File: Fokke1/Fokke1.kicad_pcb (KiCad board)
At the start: 2 copper layers, 209 x 112 mm, 101 parts, among them J101 Conn_01x20_Male, J11 Conn_01x05_Male, J12 Conn_01x05_Male, J401 Conn_01x10_Male, J403 Conn_01x10_Male, SW101 SW_SPST, SW102 SW_SPST, SW103 SW_SPST, SW104 SW_SPST, SW105 SW_SPST, SW106 SW_SPST, SW107 SW_SPST, SW108 SW_SPST, SW109 SW_SPST, SW11 SW_SPST, U11 MAX485E, U12 24LC256, U13 ATmega328-A, U14 HEADER_3x2, U26 L78L05_SOT89, U501 XC6206PxxxMR, Y11 crystal_arduino

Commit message: added logo and layout plans
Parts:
- removed C11: 100n, Capacitor_SMD:C_0603_1608Metric_Pad1.08x0.95mm_HandSolder
- removed C12, C30: 100nF, Capacitor_SMD:C_0603_1608Metric_Pad1.08x0.95mm_HandSolder
- removed C13, C14: 12pF, Capacitor_SMD:C_0402_1005Metric_Pad0.74x0.62mm_HandSolder
- removed C29: 330nF, Capacitor_SMD:C_0603_1608Metric_Pad1.08x0.95mm_HandSolder
- removed C31: 100uF, Capacitor_SMD:C_1206_3216Metric_Pad1.33x1.80mm_HandSolder
- removed C501, C502: 1uF, Capacitor_SMD:C_0603_1608Metric_Pad1.08x0.95mm_HandSolder
- removed D11: LED, LED_SMD:LED_0805_2012Metric_Pad1.15x1.40mm_HandSolder
- removed J101: Conn_01x20_Male, Connector_PinHeader_2.54mm:PinHeader_1x20_P2.54mm_Vertical
- removed J11, J12: Conn_01x05_Male, custom_kicad_lib_sk:castellated_2.54mm_01x06
- removed J401, J403: Conn_01x10_Male, custom_kicad_lib_sk:castellated_2.54mm_01x10
- removed R101, R102, R103, R104, R107, R108, R109: R, Resistor_SMD:R_0805_2012Metric_Pad1.20x1.40mm_HandSolder
- removed R11, R13: 10k, Resistor_SMD:R_0402_1005Metric_Pad0.72x0.64mm_HandSolder
- removed R12: 6k2, Resistor_SMD:R_0603_1608Metric_Pad0.98x0.95mm_HandSolder
- removed R301, R302, R303: 10k, Resistor_SMD:R_0402_1005Metric
- removed R601, R602: 4k7, Resistor_SMD:R_0603_1608Metric
- removed the REF** at (32.5, 129.5)
- removed the REF** at (173.0, 129.5)
- removed the REF** at (234.5, 72.5)
- removed the REF** at (32.5, 72.5)
- removed the REF** at (234.5, 129.5)
- removed the REF** at (100.0, 72.5)
- removed the REF** at (100.0, 129.5)
- removed the REF** at (173.0, 72.5)
- removed the REF** at (200.0, 123.0)
- removed SW11: SW_SPST, Button_Switch_SMD:SW_SPST_SKQG_WithStem
- removed U11: MAX485E, Package_SO:SOIC-8_3.9x4.9mm_P1.27mm
- removed U12: 24LC256, Package_SO:SOIC-8_3.9x4.9mm_P1.27mm
- removed U13: ATmega328-A, Package_QFP:TQFP-32_7x7mm_P0.8mm
- removed U14: HEADER_3x2, Connector_PinSocket_1.27mm:PinSocket_2x03_P1.27mm_Vertical
- removed U26: L78L05_SOT89, Package_TO_SOT_SMD:SOT-89-3
- removed U501: XC6206PxxxMR, Package_TO_SOT_SMD:SOT-23
- removed Y11: crystal_arduino, custom_kicad_lib_sk:crystal_arduino
- added G***: LOGO, kicad_images:Train-Science logo small, F.Cu at (36.0, 120.5)
- added REF**: PinHeader_2x20_P2.00mm_Vertical_SMD, Connector_PinHeader_2.00mm:PinHeader_2x20_P2.00mm_Vertical_SMD, B.Cu at (122.5, 83.5)
- R105: value R -> 100R
- moved R105 77.3 mm to (220.8, 115.5)
- moved R106 76.1 mm to (221.0, 121.0)
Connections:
- D106 pad 1: (no net) -> GPIO6 (x16)
- D106 pad 2: (no net) -> Net-(D106-Pad2) (x16)
- D107 pad 1: (no net) -> GPIO7 (x4)
- D107 pad 2: (no net) -> Net-(D107-Pad2) (x4)
- D109 pad 1: (no net) -> GPIO9 (x5)
- D109 pad 2: (no net) -> Net-(D109-Pad2) (x5)
- SW101 pad 1: (no net) -> GND (x3)
- SW101 pad 2: (no net) -> GPIO1 (x3)
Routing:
- net (no net): track 237.6 -> 0.00 mm, vias 12 -> 0
- net +5V: track 97.1 -> 0.00 mm, vias 7 -> 0
- net GPIO11: track 18.8 -> 0.00 mm
- net GPIO2: track 18.8 -> 0.00 mm, vias 2 -> 0
- net GPIO6: track 16.5 -> 0.00 mm
- net GPIO5: track 16.3 -> 0.00 mm
- net GPIO13: track 15.9 -> 0.00 mm, vias 2 -> 0
- net GPIO9: track 15.6 -> 0.00 mm, vias 2 -> 0
- net GPIO7: track 15.6 -> 0.00 mm
- net GPIO8: track 14.7 -> 0.00 mm
- net GPIO12: track 13.3 -> 0.00 mm, vias 2 -> 0
- net GPIO3: track 12.7 -> 0.00 mm
- net GPIO4: track 10.8 -> 0.00 mm
- net GPIO10: track 9.35 -> 0.00 mm
- net +3V3: track 8.18 -> 0.00 mm
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- removed copper zone on B.Cu, net GND
- removed copper zone on F.Cu, net GND
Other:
- board size 209 x 112 mm -> 209 x 64 mm
- board text removed: "3V3"
- board text removed: "5V"
- board text removed: "A"
- board text removed: "A0"
- board text removed: "A1"
- board text removed: "A2"
- board text removed: "A3"
- board text removed: "B"
- board text removed: "D10"
- board text removed: "D11"
- board text removed: "D12"
- board text removed: "D13"
- board text removed: "D2"
- board text removed: "D3"
- board text removed: "D4"
- board text removed: "D5"
- board text removed: "D6"
- board text removed: "D7"
- board text removed: "D8"
- board text removed: "D9"
- board text removed: "GND"
- board text removed: "ICSP"
- board text removed: "RES"
- board text removed: "RX"
- board text removed: "SCL"
- board text removed: "SDA"
- board text removed: "TX"
- board text removed: "Train-Science"
- board text removed: "Vin"

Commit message: I am halfway of schematic of Fokke1. I need to make me new footprints for leds and resistors and switches because I want to remove and add certain silk texts
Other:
- board text added: "1"
- board text added: "10"
- board text added: "11"
- board text added: "12"
- board text added: "2"
- board text added: "3"
- board text added: "4"
- board text added: "5"
- board text added: "6"
- board text added: "7"
- board text added: "8"
- board text added: "9"
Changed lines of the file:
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@@
   (gr_rect (start 30 76) (end 237 126) (layer "F.SilkS") (width 0.15) (fill none))
   (gr_rect (start 238 69) (end 29 133) (layer "Edge.Cuts") (width 0.1) (fill none))
+  (gr_text "10" (at 187.5 124.5) (layer "Dwgs.User")
+    (effects (font (size 1 1) (thickness 0.15)))
+  )
+  (gr_text "7" (at 161 94.5) (layer "Dwgs.User")
+    (effects (font (size 1 1) (thickness 0.15)))
+  )
+  (gr_text "9" (at 197.5 118) (layer "Dwgs.User")
+    (effects (font (size 1 1) (thickness 0.15)))
+  )
+  (gr_text "10" (at 190.5 88.5) (layer "Dwgs.User")
+    (effects (font (size 1 1) (thickness 0.15)))
+  )
+  (gr_text "1" (at 58 94) (layer "Dwgs.User")
+    (effects (font (size 1 1) (thickness 0.15)))
+  )
+  (gr_text "7" (at 154 80) (layer "Dwgs.User")
+    (effects (font (size 1 1) (thickness 0.15)))
+  )
+  (gr_text "6" (at 100 109) (layer "Dwgs.User")
+    (effects (font (size 1 1) (thickness 0.15)))
+  )
+  (gr_text "5" (at 142.5 102) (layer "Dwgs.User")
+    (effects (font (size 1 1) (thickness 0.15)))
+  )
+  (gr_text "12" (at 232 101.5) (layer "Dwgs.User")
+    (effects (font (size 1 1) (thickness 0.15)))
+  )
+  (gr_text "11" (at 232 80.5) (layer "Dwgs.User")
+    (effects (font (size 1 1) (thickness 0.15)))
+  )
+  (gr_text "4" (at 64.5 113) (layer "Dwgs.User")
+    (effects (font (size 1 1) (thickness 0.15)))
+  )
+  (gr_text "4" (at 147 93.5) (layer "Dwgs.User")
+    (effects (font (size 1 1) (thickness 0.15)))
+  )
+  (gr_text "8" (at 192.5 100.5) (layer "Dwgs.User")
+    (effects (font (size 1 1) (thickness 0.15)))
+  )
+  (gr_text "2" (at 39 109.5) (layer "Dwgs.User")
+    (effects (font (size 1 1) (thickness 0.15)))
+  )
+  (gr_text "1" (at 39 89.5) (layer "Dwgs.User")
+    (effects (font (size 1 1) (thickness 0.15)))
+  )
+  (gr_text "2" (at 74.5 106.5) (layer "Dwgs.User")
+    (effects (font (size 1 1) (thickness 0.15)))
+  )
+  (gr_text "6" (at 152 100.5) (layer "Dwgs.User")
+    (effects (font (size 1 1) (thickness 0.15)))
+  )
+  (gr_text "3" (at 111.5 117) (layer "Dwgs.User")
+    (effects (font (size 1 1) (thickness 0.15)))
+  )
+  (gr_text "5" (at 99.5 90) (layer "Dwgs.User")
+    (effects (font (size 1 1) (thickness 0.15)))
+  )
+  (gr_text "9" (at 148.5 122) (layer "Dwgs.User")
+    (effects (font (size 1 1) (thickness 0.15)))
+  )
+  (gr_text "3" (at 68 87) (layer "Dwgs.User")
+    (effects (font (size 1 1) (thickness 0.15)))
+  )
+  (gr_text "8\n" (at 170.980384 98.945766) (layer "Dwgs.User")
+    (effects (font (size 1 1) (thickness 0.15)))
+  )
 )

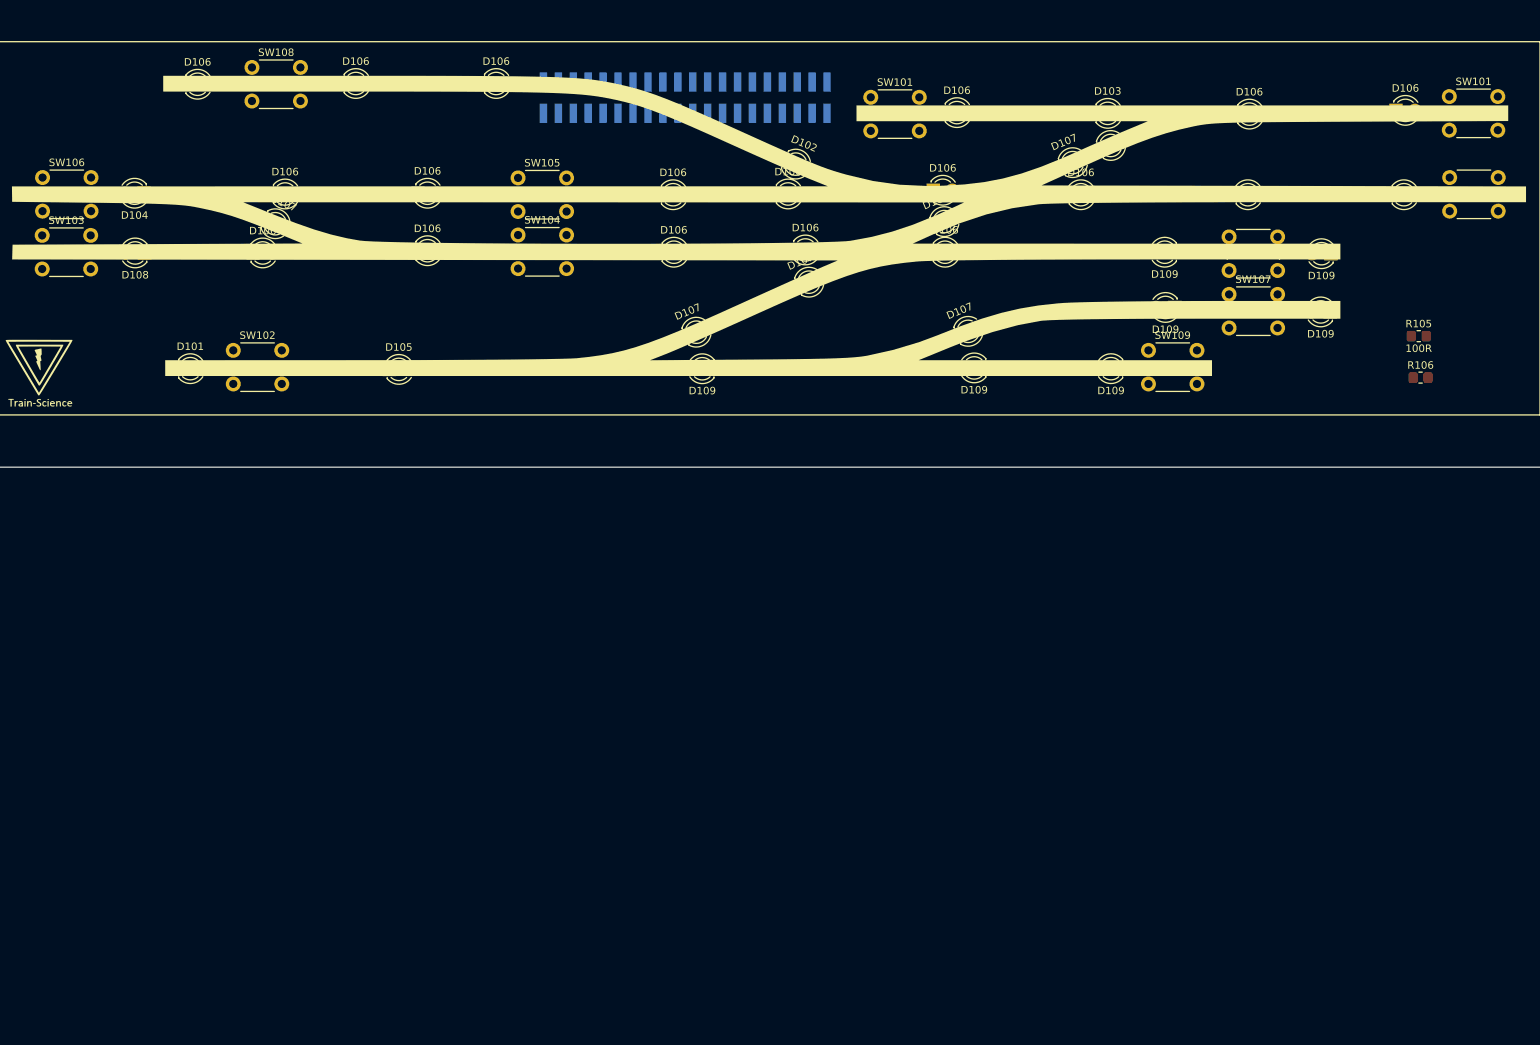
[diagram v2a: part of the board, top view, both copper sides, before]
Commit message: Did all component numbering for Fokke1. The connector is still to be finished
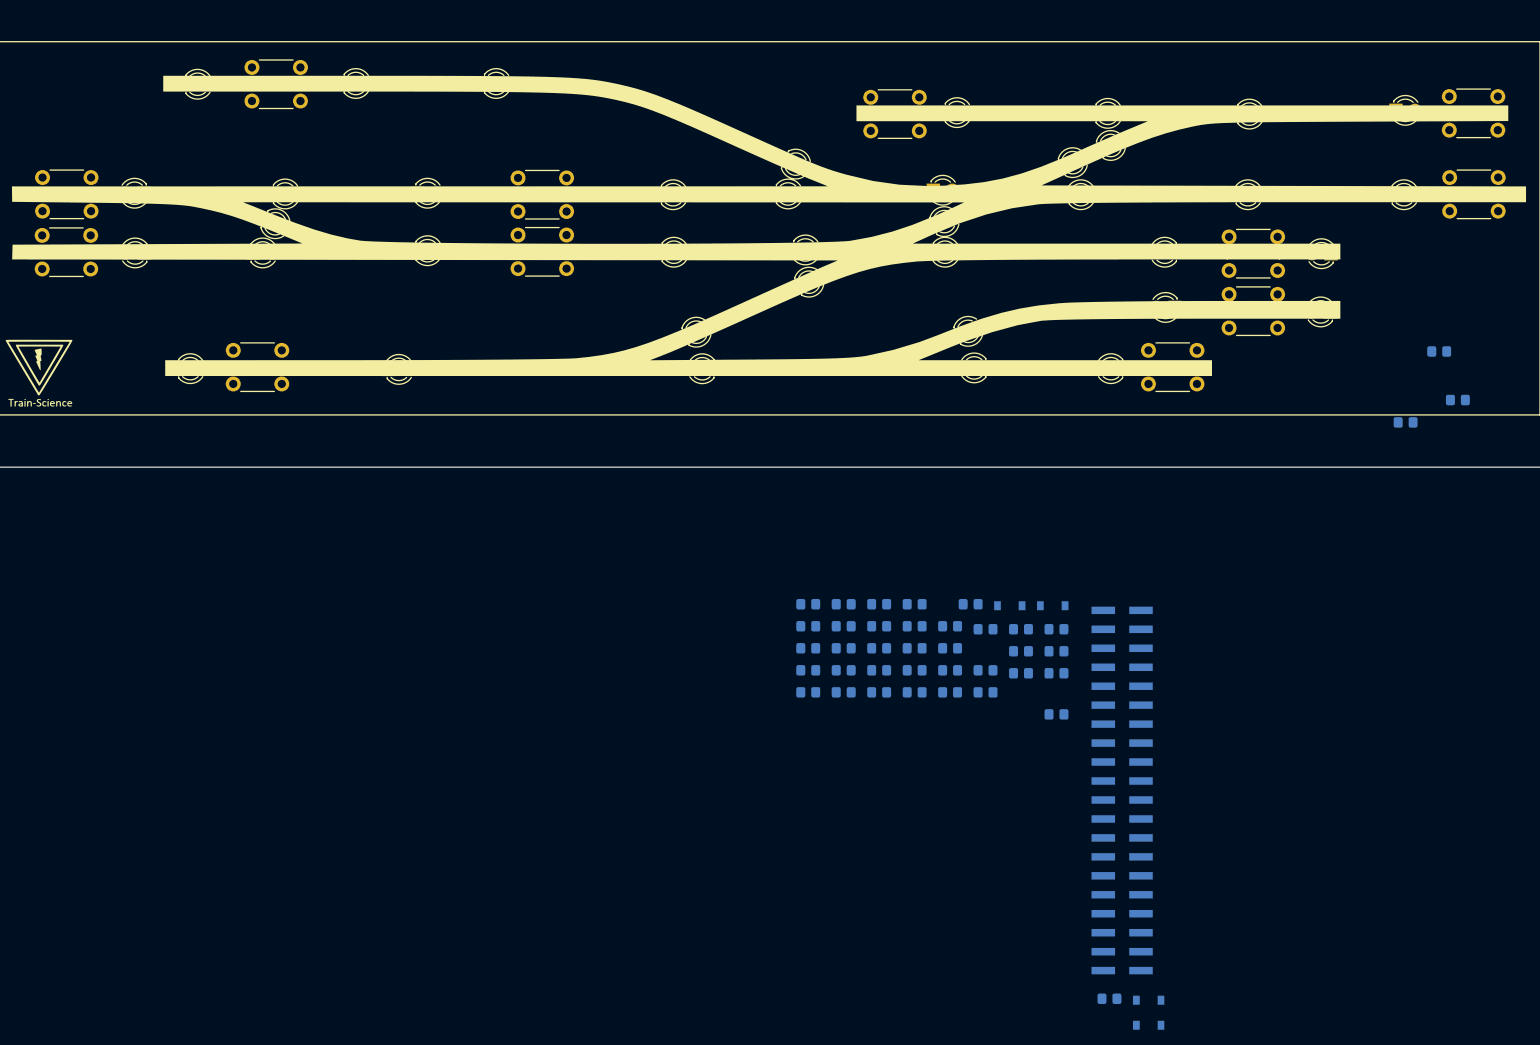
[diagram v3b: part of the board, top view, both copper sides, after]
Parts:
- removed R105: 100R, Resistor_SMD:R_0805_2012Metric_Pad1.20x1.40mm_HandSolder
- removed R106: R, Resistor_SMD:R_0805_2012Metric_Pad1.20x1.40mm_HandSolder
- removed REF**: PinHeader_2x20_P2.00mm_Vertical_SMD, Connector_PinHeader_2.00mm:PinHeader_2x20_P2.00mm_Vertical_SMD
- added D3: D, Diode_SMD:D_SOD-123, B.Cu at (166.0, 151.6)
- added D4: D, Diode_SMD:D_SOD-123, B.Cu at (184.6, 204.4)
- added D5: D, Diode_SMD:D_SOD-123, B.Cu at (171.7, 151.6)
- added D6: D, Diode_SMD:D_SOD-123, B.Cu at (184.6, 207.8)
- added J1: Conn_02x20_Top_Bottom, Connector_PinHeader_2.54mm:PinHeader_2x20_P2.54mm_Vertical_SMD, B.Cu at (181.0, 176.3)
- added R1: 1k5, custom_kicad_lib_sk:R_0805_SILK_VALUE, B.Cu at (226.0, 124.0)
- added R10: 1k5, custom_kicad_lib_sk:R_0805_SILK_VALUE, B.Cu at (158.0, 157.3)
- added R111: 1k5, custom_kicad_lib_sk:R_0805_SILK_VALUE, B.Cu at (139.0, 163.2)
- added R112: 1k5, custom_kicad_lib_sk:R_0805_SILK_VALUE, B.Cu at (160.7, 151.4)
- added R121: 1k5, custom_kicad_lib_sk:R_0805_SILK_VALUE, B.Cu at (139.0, 151.4)
- added R122: 1k5, custom_kicad_lib_sk:R_0805_SILK_VALUE, B.Cu at (172.2, 160.6)
- added R132: 3k3, custom_kicad_lib_sk:R_0805_SILK_VALUE, B.Cu at (172.2, 166.1)
- added R142: 3k3, custom_kicad_lib_sk:R_0805_SILK_VALUE, B.Cu at (148.5, 157.3)
- added R151: 1k5, custom_kicad_lib_sk:R_0805_SILK_VALUE, B.Cu at (219.0, 127.0)
- added R152: 3k3, custom_kicad_lib_sk:R_0805_SILK_VALUE, B.Cu at (223.5, 117.5)
- added R161: 1k5, custom_kicad_lib_sk:R_0805_SILK_VALUE, B.Cu at (148.5, 163.2)
- added R162: 3k3, custom_kicad_lib_sk:R_0805_SILK_VALUE, B.Cu at (153.2, 151.4)
- added R171: 1k5, custom_kicad_lib_sk:R_0805_SILK_VALUE, B.Cu at (162.7, 154.7)
- added R172: 3k3, custom_kicad_lib_sk:R_0805_SILK_VALUE, B.Cu at (139.0, 154.3)
- added R1819: 1k, custom_kicad_lib_sk:R_0805_SILK_VALUE, B.Cu at (162.7, 160.2)
- added R182: 3k3, custom_kicad_lib_sk:R_0805_SILK_VALUE, B.Cu at (143.7, 157.3)
- added R192: 3k3, custom_kicad_lib_sk:R_0805_SILK_VALUE, B.Cu at (172.2, 157.7)
- added R2: 1k5, custom_kicad_lib_sk:R_0805_SILK_VALUE, B.Cu at (162.7, 163.2)
- added R201: 1k5, custom_kicad_lib_sk:R_0805_SILK_VALUE, B.Cu at (167.5, 157.7)
- added R202: 3k3, custom_kicad_lib_sk:R_0805_SILK_VALUE, B.Cu at (172.2, 154.7)
- added R211: 1k5, custom_kicad_lib_sk:R_0805_SILK_VALUE, B.Cu at (158.0, 163.2)
- added R212: 3k3, custom_kicad_lib_sk:R_0805_SILK_VALUE, B.Cu at (179.3, 204.2)
- added R221: 1k5, custom_kicad_lib_sk:R_0805_SILK_VALUE, B.Cu at (153.2, 154.3)
- added R222: 3k3, custom_kicad_lib_sk:R_0805_SILK_VALUE, B.Cu at (143.7, 154.3)
- added R3: 1k, custom_kicad_lib_sk:R_0805_SILK_VALUE, B.Cu at (153.2, 160.2)
- added R31: 1k5, custom_kicad_lib_sk:R_0805_SILK_VALUE, B.Cu at (153.2, 157.3)
- added R32: 1k5, custom_kicad_lib_sk:R_0805_SILK_VALUE, B.Cu at (148.5, 160.2)
- added R33: 1k5, custom_kicad_lib_sk:R_0805_SILK_VALUE, B.Cu at (158.0, 154.3)
- added R41: 1k5, custom_kicad_lib_sk:R_0805_SILK_VALUE, B.Cu at (148.5, 154.3)
- added R42: 1k5, custom_kicad_lib_sk:R_0805_SILK_VALUE, B.Cu at (143.7, 151.4)
- added R51: 1k5, custom_kicad_lib_sk:R_0805_SILK_VALUE, B.Cu at (167.5, 160.6)
- added R52: 1k5, custom_kicad_lib_sk:R_0805_SILK_VALUE, B.Cu at (167.5, 154.7)
- added R61: 1k5, custom_kicad_lib_sk:R_0805_SILK_VALUE, B.Cu at (139.0, 160.2)
- added R62: 1k5, custom_kicad_lib_sk:R_0805_SILK_VALUE, B.Cu at (153.2, 163.2)
- added R7: 1k5, custom_kicad_lib_sk:R_0805_SILK_VALUE, B.Cu at (158.0, 160.2)
- added R81: 1k5, custom_kicad_lib_sk:R_0805_SILK_VALUE, B.Cu at (143.7, 160.2)
- added R82: 1k5, custom_kicad_lib_sk:R_0805_SILK_VALUE, B.Cu at (148.5, 151.4)
- added R91: 1k5, custom_kicad_lib_sk:R_0805_SILK_VALUE, B.Cu at (139.0, 157.3)
- added R92: 1k5, custom_kicad_lib_sk:R_0805_SILK_VALUE, B.Cu at (143.7, 163.2)
- D1: renamed from D104; footprint LED_THT:LED_D3.0mm -> custom_kicad_lib_sk:LED_NO_SILK
- D10, D152, D212, D81, D82, D91, D92: renamed from D109; footprint LED_THT:LED_D3.0mm -> custom_kicad_lib_sk:LED_NO_SILK
- D111, D112, D121, D122, D132, D142, D162, D171, D182, D192, D202, D31, D32, D33, D51, D52, D61, D62, D7: renamed from D106; footprint LED_THT:LED_D3.0mm -> custom_kicad_lib_sk:LED_NO_SILK
- D1314, D151, D172, D1819, D201, D211, D221: renamed from D107; footprint LED_THT:LED_D3.0mm -> custom_kicad_lib_sk:LED_NO_SILK
- D161: renamed from D102; footprint LED_THT:LED_D3.0mm -> custom_kicad_lib_sk:LED_NO_SILK
- D2: renamed from D108; footprint LED_THT:LED_D3.0mm -> custom_kicad_lib_sk:LED_NO_SILK
- D222: renamed from D103; footprint LED_THT:LED_D3.0mm -> custom_kicad_lib_sk:LED_NO_SILK
- D41: renamed from D101; footprint LED_THT:LED_D3.0mm -> custom_kicad_lib_sk:LED_NO_SILK
- D42: renamed from D105; footprint LED_THT:LED_D3.0mm -> custom_kicad_lib_sk:LED_NO_SILK
- SW1: renamed from SW106; footprint Button_Switch_THT:SW_PUSH_6mm_H4.3mm -> custom_kicad_lib_sk:SW_NO_SILK
- SW10: renamed from SW109; footprint Button_Switch_THT:SW_PUSH_6mm_H4.3mm -> custom_kicad_lib_sk:SW_NO_SILK
- SW11, SW12, SW7, SW8: renamed from SW101; footprint Button_Switch_THT:SW_PUSH_6mm_H4.3mm -> custom_kicad_lib_sk:SW_NO_SILK
- SW2: renamed from SW103; footprint Button_Switch_THT:SW_PUSH_6mm_H4.3mm -> custom_kicad_lib_sk:SW_NO_SILK
- SW3: renamed from SW108; footprint Button_Switch_THT:SW_PUSH_6mm_H4.3mm -> custom_kicad_lib_sk:SW_NO_SILK
- SW4: renamed from SW102; footprint Button_Switch_THT:SW_PUSH_6mm_H4.3mm -> custom_kicad_lib_sk:SW_NO_SILK
- SW5: renamed from SW105; footprint Button_Switch_THT:SW_PUSH_6mm_H4.3mm -> custom_kicad_lib_sk:SW_NO_SILK
- SW6: renamed from SW104; footprint Button_Switch_THT:SW_PUSH_6mm_H4.3mm -> custom_kicad_lib_sk:SW_NO_SILK
- SW9: renamed from SW107; footprint Button_Switch_THT:SW_PUSH_6mm_H4.3mm -> custom_kicad_lib_sk:SW_NO_SILK
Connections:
- D1 pad 1: GPIO4 -> GPIO1
- D10 pad 1: GPIO9 -> GPIO10
- D10 pad 2: Net-(D109-Pad2) -> Net-(D10-Pad2)
- D111 pad 1: GPIO6 -> GPIO11
- D111 pad 2: Net-(D106-Pad2) -> Net-(D111-Pad2)
- D112 pad 1: GPIO6 -> GPIO11
- D112 pad 2: Net-(D106-Pad2) -> Net-(D112-Pad2)
- D121 pad 1: GPIO6 -> GPIO12
- D121 pad 2: Net-(D106-Pad2) -> Net-(D121-Pad2)
- D122 pad 1: GPIO6 -> GPIO12
- D122 pad 2: Net-(D106-Pad2) -> Net-(D122-Pad2)
- D1314 pad 1: GPIO7 -> Net-(D1314-Pad1)
- D1314 pad 2: Net-(D107-Pad2) -> Net-(D1314-Pad2)
- D132 pad 1: GPIO6 -> GND
- D132 pad 2: Net-(D106-Pad2) -> Net-(R132-Pad2)
- D142 pad 1: GPIO6 -> GND
- D142 pad 2: Net-(D106-Pad2) -> Net-(D142-Pad2)
- D151 pad 1: GPIO7 -> GPIO15
- D151 pad 2: Net-(D107-Pad2) -> Net-(R151-Pad2)
- D152 pad 1: GPIO9 -> GND
- D152 pad 2: Net-(D109-Pad2) -> Net-(R152-Pad2)
- D161 pad 1: GPIO2 -> GPIO16
- D162 pad 1: GPIO6 -> GND
- D162 pad 2: Net-(D106-Pad2) -> Net-(R162-Pad2)
- D171 pad 1: GPIO6 -> GPIO17
- D171 pad 2: Net-(D106-Pad2) -> Net-(D171-Pad2)
- D172 pad 1: GPIO7 -> GND
- D172 pad 2: Net-(D107-Pad2) -> Net-(R172-Pad2)
- D1819 pad 1: GPIO7 -> Net-(D1819-Pad1)
- D1819 pad 2: Net-(D107-Pad2) -> Net-(R1819-Pad2)
- D182 pad 1: GPIO6 -> GND
- D182 pad 2: Net-(D106-Pad2) -> Net-(R182-Pad2)
- D192 pad 1: GPIO6 -> GND
- D192 pad 2: Net-(D106-Pad2) -> Net-(D192-Pad2)
- D2 pad 1: GPIO8 -> GPIO2
- D201 pad 1: GPIO7 -> GPIO20
- D201 pad 2: Net-(D107-Pad2) -> Net-(R201-Pad2)
- D202 pad 1: GPIO6 -> GND
- D202 pad 2: Net-(D106-Pad2) -> Net-(R202-Pad2)
- D211 pad 1: GPIO7 -> GPIO21
- D211 pad 2: Net-(D107-Pad2) -> Net-(R211-Pad2)
- D212 pad 1: GPIO9 -> GND
- D212 pad 2: Net-(D109-Pad2) -> Net-(R212-Pad2)
- D221 pad 1: GPIO7 -> GPIO22
- D221 pad 2: Net-(D107-Pad2) -> Net-(R221-Pad2)
- D222 pad 1: GPIO3 -> GND
- D31 pad 1: GPIO6 -> GPIO3
- D31 pad 2: Net-(D106-Pad2) -> Net-(D31-Pad2)
- D32 pad 1: GPIO6 -> GPIO3
- D32 pad 2: Net-(D106-Pad2) -> Net-(D32-Pad2)
- D33 pad 1: GPIO6 -> GPIO3
- D33 pad 2: Net-(D106-Pad2) -> Net-(D33-Pad2)
- D41 pad 1: GPIO1 -> GPIO4
- D42 pad 1: GPIO5 -> GPIO4
- D51 pad 1: GPIO6 -> GPIO5
- D51 pad 2: Net-(D106-Pad2) -> Net-(D51-Pad2)
- D52 pad 1: GPIO6 -> GPIO5
- D52 pad 2: Net-(D106-Pad2) -> Net-(D52-Pad2)
- D61 pad 2: Net-(D106-Pad2) -> Net-(D61-Pad2)
- D62 pad 2: Net-(D106-Pad2) -> Net-(D62-Pad2)
- D7 pad 1: GPIO6 -> GPIO7
- D7 pad 2: Net-(D106-Pad2) -> Net-(D7-Pad2)
- D81 pad 1: GPIO9 -> GPIO8
- D81 pad 2: Net-(D109-Pad2) -> Net-(D81-Pad2)
- D82 pad 1: GPIO9 -> GPIO8
- D82 pad 2: Net-(D109-Pad2) -> Net-(D82-Pad2)
- D91 pad 2: Net-(D109-Pad2) -> Net-(D91-Pad2)
- D92 pad 2: Net-(D109-Pad2) -> Net-(D92-Pad2)
- SW1 pad 2: GPIO6 -> GPIO1
- SW10 pad 2: GPIO9 -> GPIO10
- SW11 pad 2: GPIO1 -> GPIO11
- SW12 pad 2: GPIO1 -> GPIO12
- SW2 pad 2: GPIO3 -> GPIO2
- SW3 pad 2: GPIO8 -> GPIO3
- SW4 pad 2: GPIO2 -> GPIO4
- SW6 pad 2: GPIO4 -> GPIO6
- SW7 pad 2: GPIO1 -> GPIO7
- SW8 pad 2: GPIO1 -> GPIO8
- SW9 pad 2: GPIO7 -> GPIO9
